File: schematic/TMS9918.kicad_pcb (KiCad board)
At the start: 2 copper layers, 74.9 x 81.3 mm, 21 parts, among them J1 Bus, J2 Video out, J3 Power, Q1 2N4401, U1 TMS9918A, U2 HM62256BLP, U3 74HCT574, U4 74HCT574, U5 74HCT574, U6 74HCT04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

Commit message: V1.1
Various improvements
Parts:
- added J4: Conn_01x04_Female, Connector_PinHeader_2.54mm:PinHeader_1x04_P2.54mm_Vertical, F.Cu at (90.2, 87.6)
- C7, C8: value 16pf -> 22pf
- Q1: value 2N4401 -> Q_NPN_EBC
- R1: value 75 -> 1k
- U2: footprint Package_DIP:DIP-28_W15.24mm_Socket -> Package_DIP:DIP-28_W15.24mm
- moved C1 16.3 mm to (106.7, 86.4)
- moved J2 7.37 mm to (108.0, 64.8), turned to 180 degrees
- moved Q1 5.46 mm to (101.0, 92.1), turned to 180 degrees
- moved R3 2.29 mm to (104.1, 89.5)
- moved R1 2.23 mm to (104.1, 93.3)
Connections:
- net /R~{W} renamed R~{W}
- net /VD0 renamed VD0
- net /VD1 renamed VD1
- net /VD2 renamed VD2
- net /VD3 renamed VD3
- net /VD4 renamed VD4
- net /VD5 renamed VD5
- net /VD6 renamed VD6
- net /VD7 renamed VD7
- net /~{R}W renamed ~{R}W
- net Net-(Q1-Pad2) renamed /vid
- U1 pad 16: /~{INT} -> unconnected-(U1-Pad16)
- U1 pad 17: /D0 -> /D7
- U1 pad 18: /D1 -> /D6
- U1 pad 19: /D2 -> /D5
- U1 pad 20: /D3 -> /D4
- U1 pad 21: /D4 -> /D3
- U1 pad 22: /D5 -> /D2
- U1 pad 23: /D6 -> /D1
- U1 pad 24: /D7 -> /D0
- U1 pad 35: /EXTVDP -> /EXT
- U1 pad 37: /GROMCLK -> Net-(U1-Pad37)
- U1 pad 38: /CPUCLK -> Net-(U1-Pad38)
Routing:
- net /D2: track 5.60 -> 26.2 mm
- net /D1: track 12.5 -> 28.8 mm
- net /D3: track 6.65 -> 21.9 mm
- net /D7: track 22.9 -> 8.46 mm
- net /D6: track 22.9 -> 8.46 mm
- net /D5: track 22.9 -> 8.46 mm
- net /D4: track 22.9 -> 8.46 mm
- net /D0: track 18.9 -> 31.5 mm
- net /vid: track 11.7 -> 20.7 mm
- net Net-(U1-Pad38): track 0.00 -> 3.82 mm
- net Net-(U1-Pad37): track 0.00 -> 3.82 mm
- net /EXT: track 0.00 -> 3.82 mm
- net Net-(J2-Pad2): track 33.4 -> 36.4 mm
- net VCC: track 229.4 -> 231.9 mm
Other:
- board size 74.9 x 81.3 mm -> 72.8 x 75.6 mm
- board text added: "+5V"
- board text added: "D0"
- board text added: "D1"
- board text added: "D2"
- board text added: "D3"
- board text added: "D4"
- board text added: "D5"
- board text added: "D6"
- board text added: "D7"
- board text added: "GND"
- board text added: "M"
- board text added: "OUT"
- board text added: "~{R}"
- board text added: "~{W}"

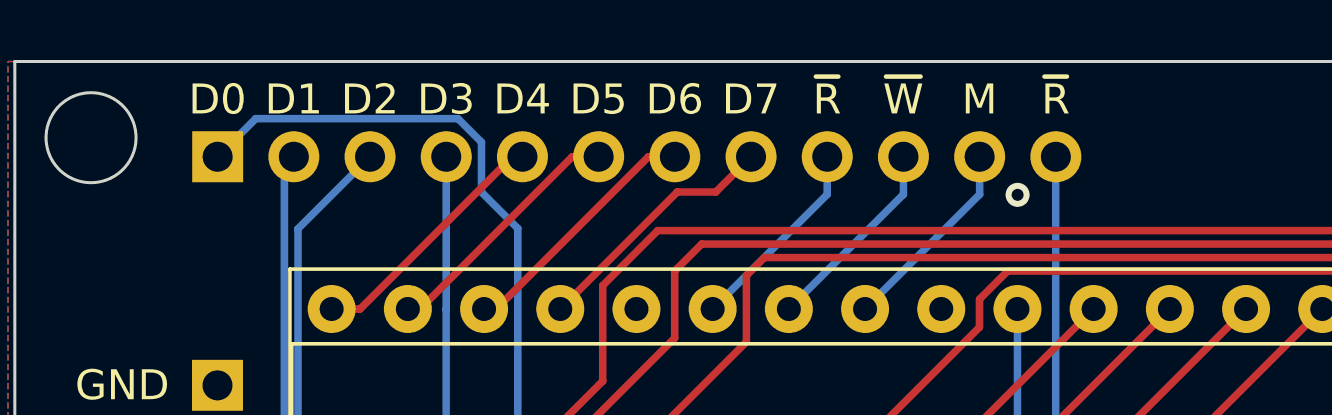
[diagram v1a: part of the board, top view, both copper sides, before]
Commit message: V1.2
Label D0..D7 order changed
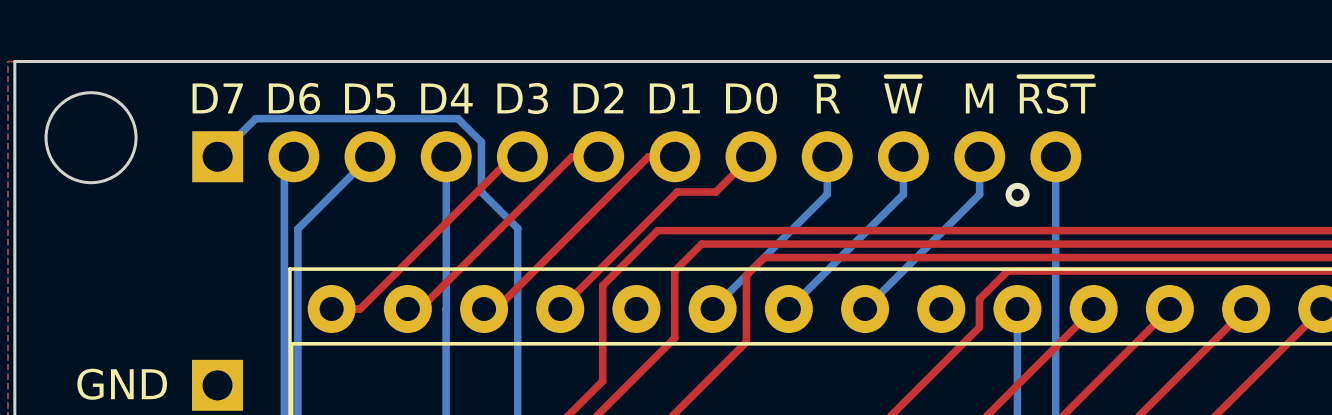
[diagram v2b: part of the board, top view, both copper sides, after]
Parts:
- Q1: value Q_NPN_EBC -> i.e. 2N4401
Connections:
- J1 pad 1: /D0 -> /D7
- J1 pad 2: /D1 -> /D6
- J1 pad 3: /D2 -> /D5
- J1 pad 4: /D3 -> /D4
- J1 pad 5: /D4 -> /D3
- J1 pad 6: /D5 -> /D2
- J1 pad 7: /D6 -> /D1
- J1 pad 8: /D7 -> /D0
- U1 pad 17: /D7 -> /D0
- U1 pad 18: /D6 -> /D1
- U1 pad 19: /D5 -> /D2
- U1 pad 20: /D4 -> /D3
- U1 pad 21: /D3 -> /D4
- U1 pad 22: /D2 -> /D5
- U1 pad 23: /D1 -> /D6
- U1 pad 24: /D0 -> /D7
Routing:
- net /D7: track 8.46 -> 31.5 mm
- net /D0: track 31.5 -> 8.46 mm
- net /D6: track 8.46 -> 28.8 mm
- net /D1: track 28.8 -> 8.46 mm
- net /D5: track 8.46 -> 26.2 mm
- net /D2: track 26.2 -> 8.46 mm
- net /D4: track 8.46 -> 21.9 mm
- net /D3: track 21.9 -> 8.46 mm
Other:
- board text added: "~{RST}"
